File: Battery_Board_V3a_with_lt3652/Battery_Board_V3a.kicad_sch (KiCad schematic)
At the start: 201 parts, among them IC2 PCT2075DP,118, IC3 RP2040_QFN56, IC4 LT3652IMSE#PBF, J1 Bypass, J10 Jetson, J11 BM04B-SRSS-TB(LF)(SN), J14 Solar, J15 FC, J16 I2C Multiplexer Breakout, J17 ISS Foot, J18 Screw_Terminal_01x02, J19 BM04B-SRSS-TB(LF)(SN), J2 Heater, J20 CAN1, J21 BM04B-SRSS-TB(LF)(SN), J22 CAN2, J23 Conn_ARM_JTAG_SWD_10, J24 USB_B_Micro, J25 Life Makes Lemonade, J26 BM04B-SRSS-TB(LF)(SN), J27 I2C0 Breakout, J3 BURN, J4 CHARGE, J5 Foot0, J6 Foot1, J7 Foot2, J8 Foot3, J9 RBF, K1 APAN3105, Q1 IRF7458, Q10 IRLML2803, Q11 NDS8434, Q2 IRF7458, Q3 MBT2222ADW1T1, Q4 MMBT2222AT, Q5 MBT2222ADW1T1, Q6 IRLML2803, Q7 IRLML2803, Q8 NDS8434, Q9 NDS8434, SW1 KMR2, SW2 KMR2, U1 R5460N208AA, U10 TLVH431 DBZ SOT-23, U11 MCP25625-E/ML, U12 INA219AxD, U13 MAX706RESA, U14 INA219AxD, U2 1049, U3 TPS54226PWPRPWP14_2P31X2P46-L, U4 1049, U5 TPS54226PWPRPWP14_2P31X2P46-L, U6 TPS7A4501DCQT, U7 ADS1015IDGS, U8 W25Q128JV, U9 AD8495, Y1 Crystal_GND24, Y2 Crystal_GND24

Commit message: Footprint Changes
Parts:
- C3, C4: footprint Capacitor_SMD:C_1210_3225Metric -> Capacitor_SMD:C_1206_3216Metric
- D1, D6, D9: symbol mainboard:DFLS130L -> Device:D_Schottky
- D4, D7: value D_Schottky -> DFLS130L-7; footprint Diode_SMD:D_SMB -> Diode_SMD:D_PowerDI-123
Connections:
- net VBATT_SENSE: now also D6.2 (A), D9.2 (A); no longer D6.A, D9.A
- net VBUSP: now also D1.1 (K); no longer D1.C
- net VBatt: now also D9.1 (K); no longer D9.C
- net at K1.C2, Q4.3 (C): now also D1.2 (A); no longer D1.A
- net at C39.2, IC4.11 (BOOST): now also D6.1 (K); no longer D6.C

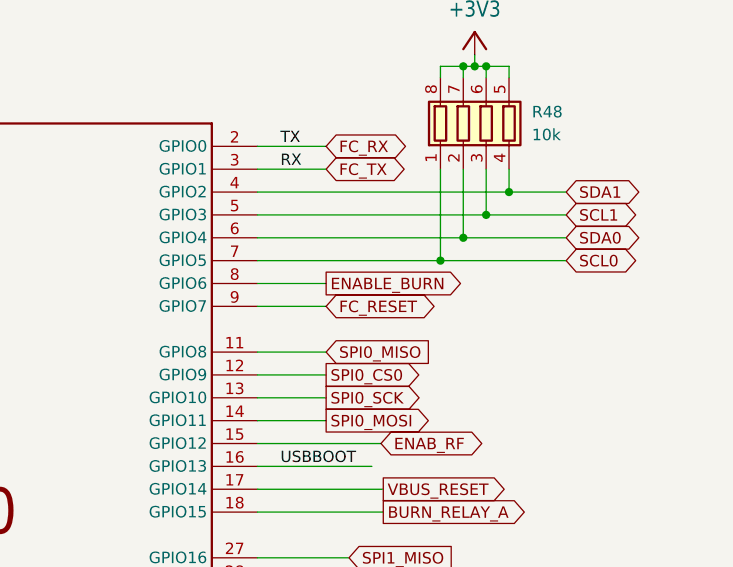
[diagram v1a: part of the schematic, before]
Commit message: [MAJOR ISSUE] Fixed Burn_Enable Issue
MAJOR ISSUE:
Burn Wire Circuit does not work on V3a due to mislabeled schematic nets. uController had Enable_Burn rather than ENAB_Burn. Change was make so not uController connects to the ENAB_Burn
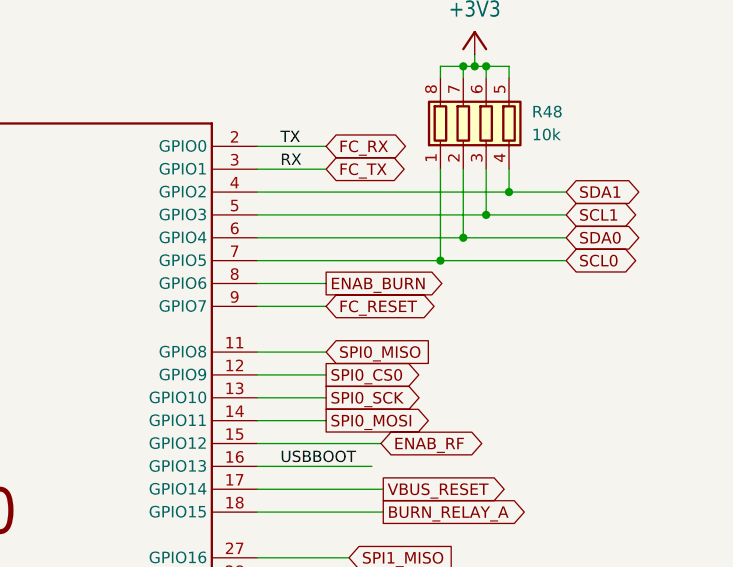
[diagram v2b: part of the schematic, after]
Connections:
- net ENABLE_BURN is gone; now on net ENAB_BURN: IC3.8 (GPIO6)
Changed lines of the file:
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@@
 		)
 	)
-	(global_label "ENABLE_BURN"
+	(global_label "ENAB_BURN"
 		(shape output)
 		(at 538.48 278.13 0)
@@
 		)
 		(property "Intersheetrefs" "${INTERSHEET_REFS}"
-			(at 554.0769 278.0506 0)
+			(at 552.4719 278.13 0)
 			(effects
 				(font
